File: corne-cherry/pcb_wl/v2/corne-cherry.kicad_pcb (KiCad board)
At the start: 2 copper layers, 152.8 x 91.4 mm, 72 parts, among them J1 MJ-4PP-9, J2 OLED, J3 Conn_01x02_Female, SW1 SW_PUSH, SW10 SW_PUSH, SW11 SW_PUSH, SW12 SW_PUSH, SW13 SW_PUSH, SW14 SW_PUSH, SW15 SW_PUSH, SW16 SW_PUSH, SW17 SW_PUSH, SW18 SW_PUSH, SW19 SW_PUSH, SW2 SW_PUSH, SW20 SW_PUSH, SW21 SW_PUSH, SW22 SW_PUSH, SW23 SW_SPDT, SW24 SW_SPDT, SW3 SW_PUSH, SW4 SW_PUSH, SW5 SW_PUSH, SW6 SW_PUSH, SW7 SW_PUSH, SW8 SW_PUSH, SW9 SW_PUSH, U1 ProMicro

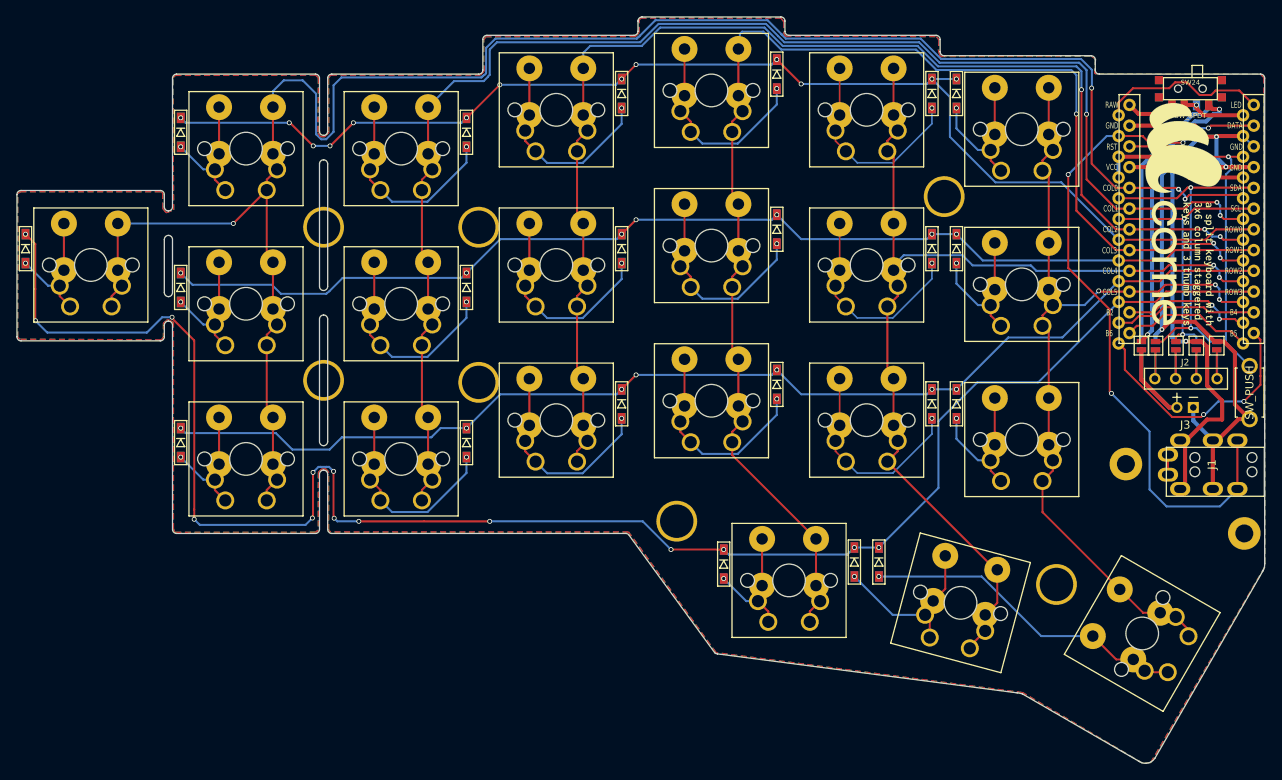
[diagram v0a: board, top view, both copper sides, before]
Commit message: Improver SI footprint, ground fills
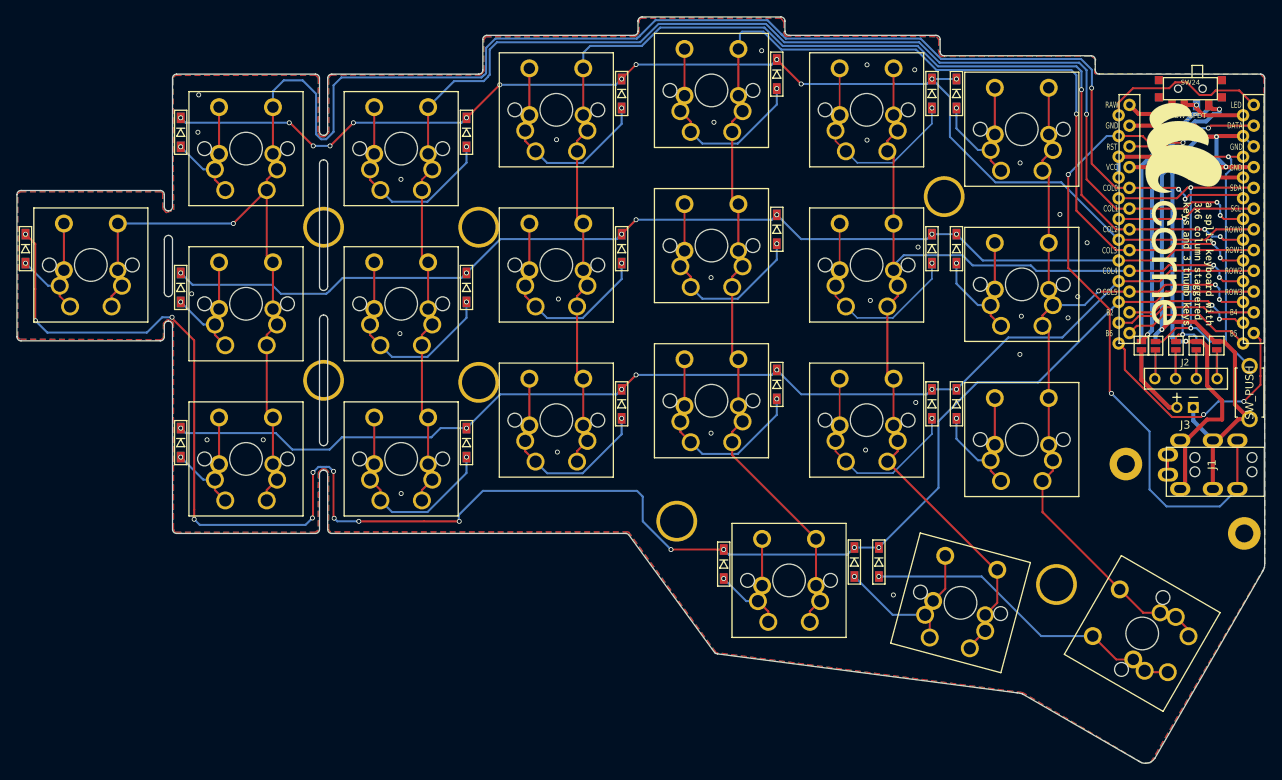
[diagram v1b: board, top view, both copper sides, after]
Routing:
- net row3: track 217.1 -> 222.5 mm
- net GND: vias 3 -> 33

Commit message: Added power switch stabilization vias
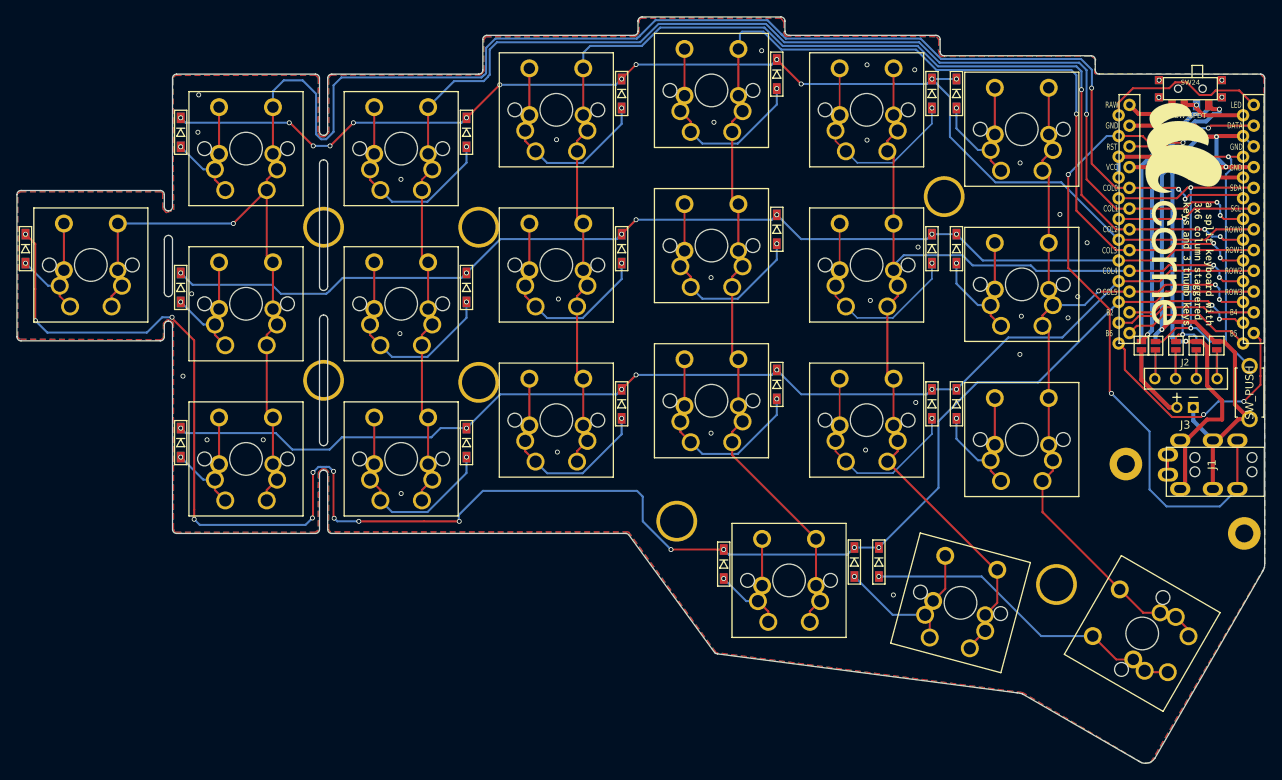
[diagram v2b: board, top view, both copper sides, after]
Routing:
- net GND: vias 33 -> 34
- net (no net): vias 0 -> 4
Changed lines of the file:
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@@
     (thickness 1.6)
     (drawings 110)
-    (tracks 989)
+    (tracks 994)
     (zones 0)
     (modules 72)
@@
   (gr_line (start 155 65.25) (end 155 63.75) (angle 90) (layer Edge.Cuts) (width 0.15))
   (gr_line (start 173.5 65.75) (end 155.5 65.75) (angle 90) (layer Edge.Cuts) (width 0.15))
+  (via (at 181.81308 68.74158) (size 0.6) (drill 0.4) (layers F.Cu B.Cu) (net 0))
+  (via (at 181.78768 70.84978) (size 0.6) (drill 0.4) (layers F.Cu B.Cu) (net 0))
+  (via (at 189.50928 70.82438) (size 0.6) (drill 0.4) (layers F.Cu B.Cu) (net 0))
+  (via (at 189.50928 68.74158) (size 0.6) (drill 0.4) (layers F.Cu B.Cu) (net 0))
   (segment (start 193.406 87.012) (end 193.4064 87.012) (width 0.25) (layer F.Cu) (net 1) (status 30))
   (segment (start 176.86 88.282) (end 187.518 88.282) (width 0.25) (layer F.Cu) (net 1) (status 10))
@@
   (via (at 172.99928 88.65518) (size 0.6) (drill 0.4) (layers F.Cu B.Cu) (net 26))
   (via (at 169.67188 85.17538) (size 0.6) (drill 0.4) (layers F.Cu B.Cu) (net 26))
+  (via (at 62.28068 104.98738) (size 0.6) (drill 0.4) (layers F.Cu B.Cu) (net 26))
   (segment (start 186.375 100.75) (end 187.05 100.75) (width 0.5) (layer F.Cu) (net 27) (status 10))
   (segment (start 187.05 100.75) (end 187.7 101.4) (width 0.5) (layer F.Cu) (net 27))

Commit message: flipped footprints
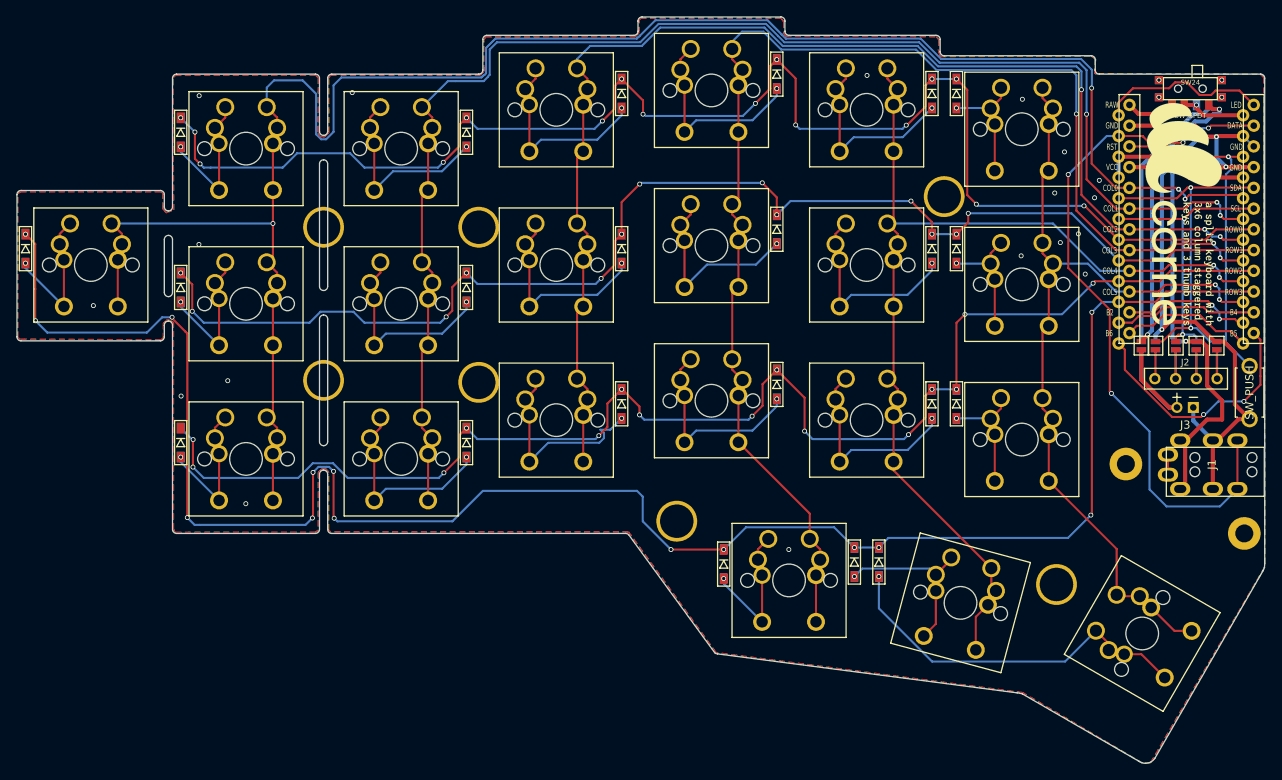
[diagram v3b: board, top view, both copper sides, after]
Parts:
- turned SW1 to 0 degrees
- turned SW10 to 0 degrees
- turned SW11 to 0 degrees
- turned SW12 to 0 degrees
- turned SW13 to 0 degrees
- turned SW14 to 0 degrees
- turned SW15 to 0 degrees
- turned SW16 to 0 degrees
- turned SW17 to 0 degrees
- turned SW18 to 0 degrees
- turned SW19 to 0 degrees
- turned SW2 to 0 degrees
- turned SW20 to 345 degrees
- turned SW21 to 60 degrees
- turned SW22 to 0 degrees
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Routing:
- net row2: track 144.0 -> 173.3 mm, vias 7 -> 15
- net row0: track 153.2 -> 180.5 mm, vias 13 -> 16
- net row1: track 139.8 -> 161.6 mm, vias 7 -> 13
- net row3: track 222.5 -> 233.6 mm
- net Net-(D21-Pad2): track 40.2 -> 46.0 mm
- net Net-(D12-Pad2): track 18.7 -> 15.1 mm
- net Net-(D6-Pad2): track 18.7 -> 15.1 mm
- net Net-(D18-Pad2): track 18.7 -> 15.1 mm
- net Net-(D19-Pad2): track 16.2 -> 18.1 mm
- net Net-(D22-Pad2): track 16.2 -> 18.1 mm
- net Net-(D7-Pad2): track 16.2 -> 18.1 mm
- net Net-(D13-Pad2): track 16.2 -> 18.1 mm
- net Net-(D1-Pad2): track 16.2 -> 18.1 mm
- net Net-(D2-Pad2): track 26.0 -> 24.4 mm
- net Net-(D10-Pad2): track 26.0 -> 24.4 mm
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
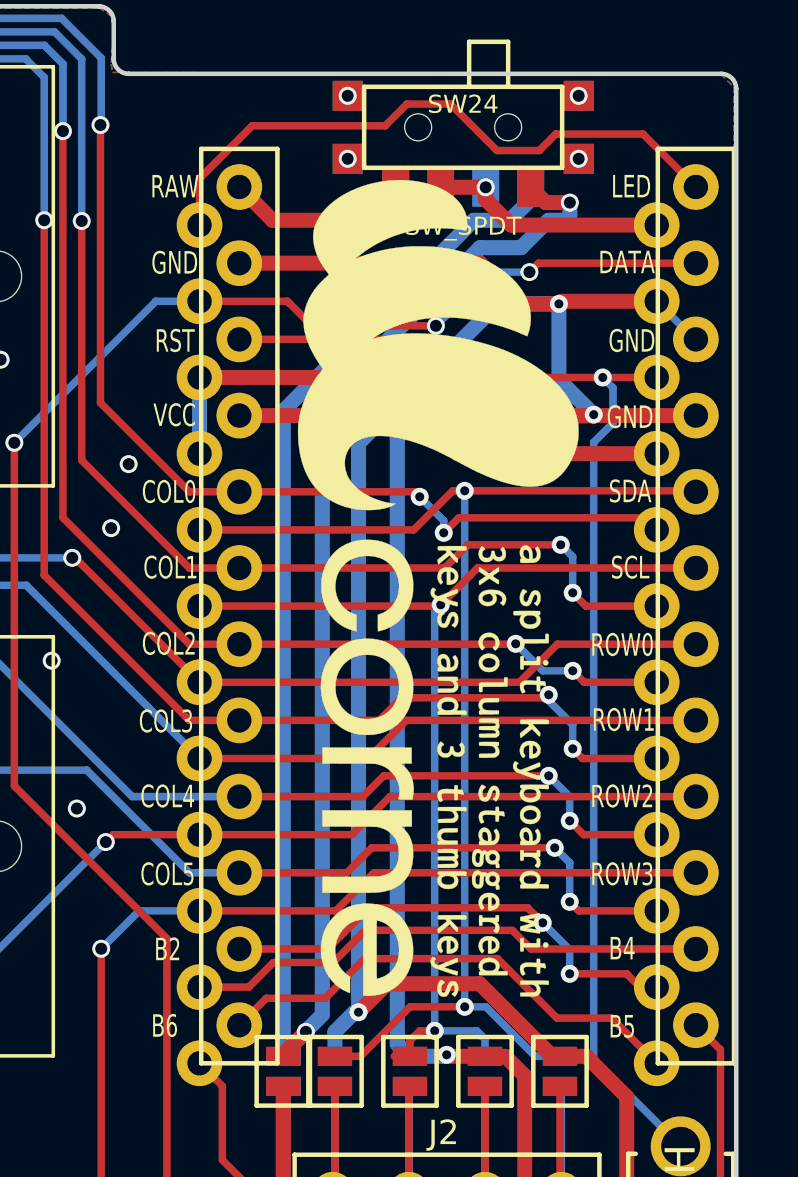
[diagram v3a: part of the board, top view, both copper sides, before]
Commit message: Added proper SPORNE logo
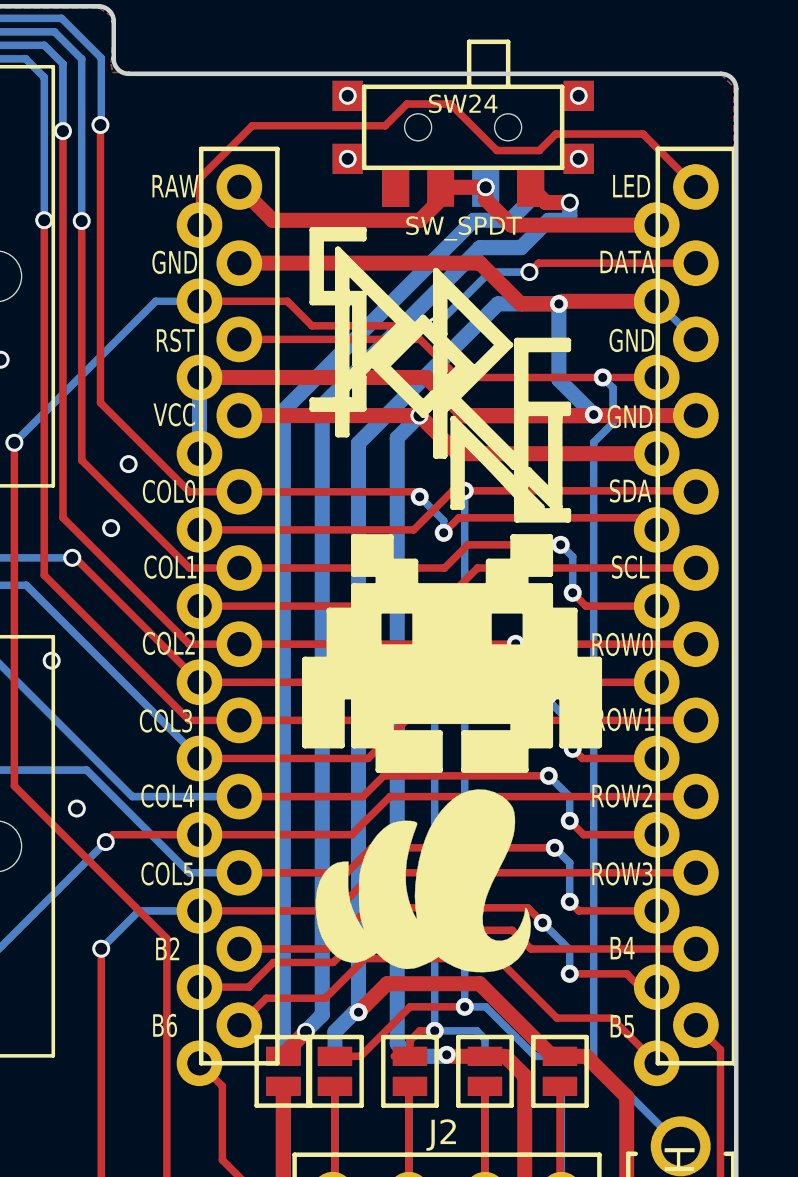
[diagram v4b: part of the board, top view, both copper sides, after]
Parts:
- added G***: LOGO, Silks:corne-logo, B.Cu at (183.9, 95.1)
- added G***: LOGO, Silks:corne-logo, F.Cu at (183.9, 95.1)
- added REF**: space-invader-logo, Silks:space-invader-logo, B.Cu at (185.1, 87.4)
- added REF**: space-invader-logo, Silks:space-invader-logo, F.Cu at (185.1, 87.4)
- G1, G2: footprint kbd:corne -> Silks:sporne-logo-small
- moved G1 6.69 mm to (185.1, 78.5), turned to 0 degrees
- moved G2 6.60 mm to (185.1, 78.5), turned to 180 degrees

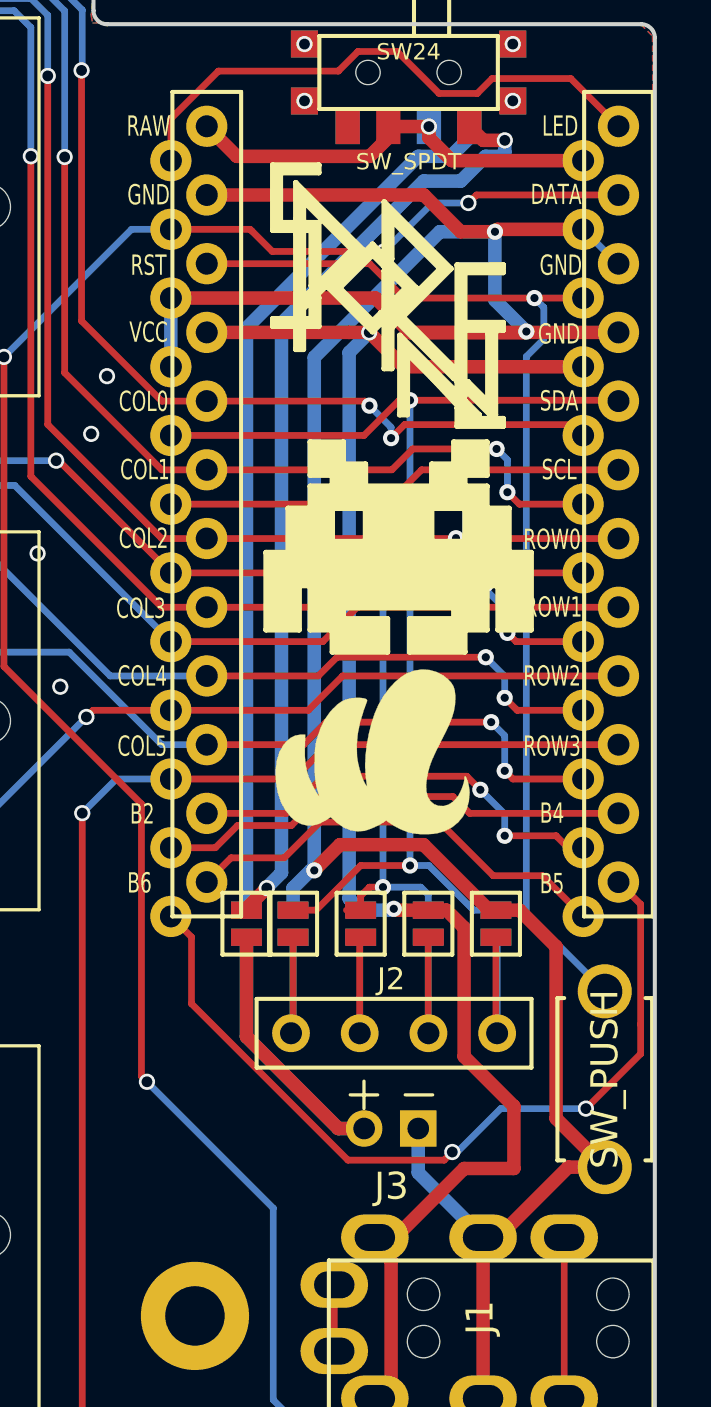
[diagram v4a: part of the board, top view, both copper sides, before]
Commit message: Logo fix
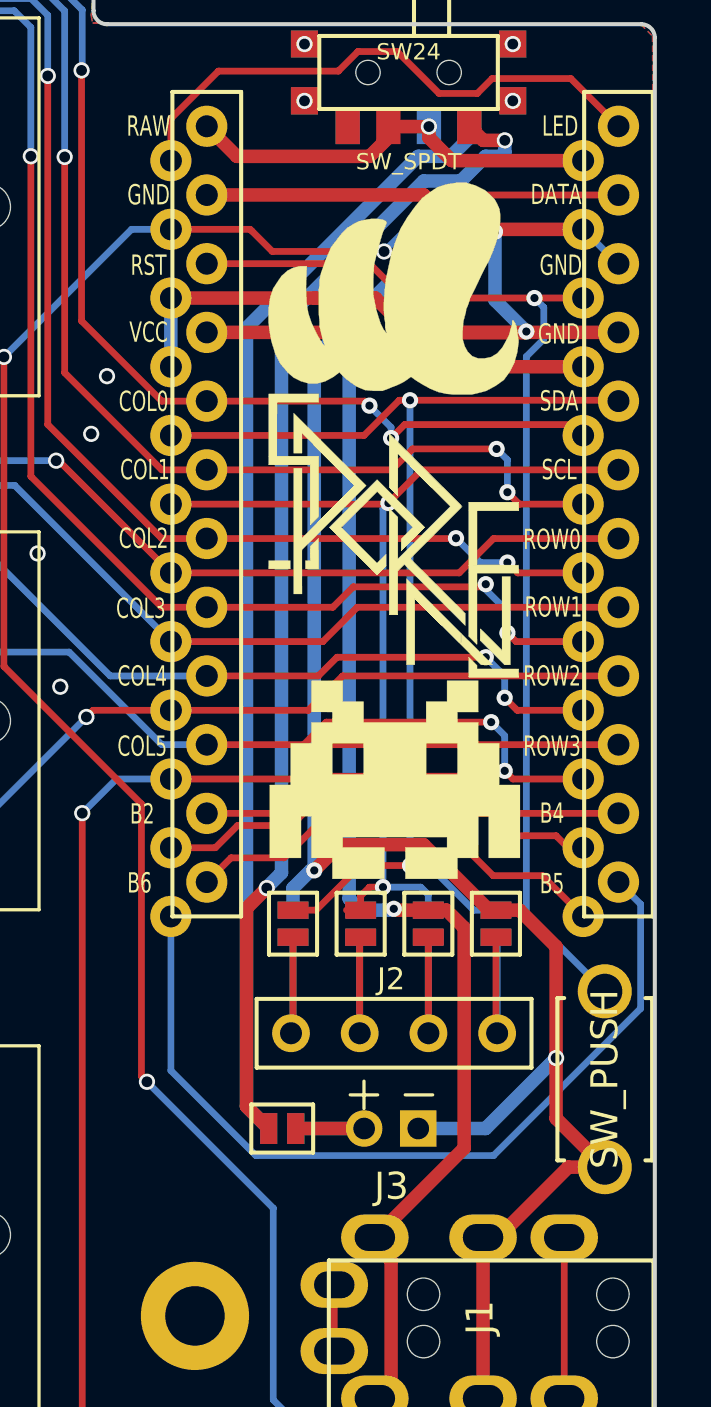
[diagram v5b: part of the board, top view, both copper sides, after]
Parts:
- removed the G*** at (183.9, 95.1) (x2)
- removed G1, G2: Logo_Open_Hardware_Small, Silks:sporne-logo-small
- removed REF** (x2): space-invader-logo, Silks:space-invader-logo
- added G***: LOGO, Silks:sporne-logo-small, B.Cu at (184.0, 86.8)
- added G***: LOGO, Silks:sporne-logo-small, F.Cu at (185.1, 86.7)
- moved JP1 7.69 mm to (181.0, 108.8), turned to 180 degrees
- moved JP10 7.69 mm to (181.0, 108.8), turned to 180 degrees
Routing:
- net Net-(J3-Pad2): track 18.9 -> 5.06 mm
- net Net-(JP10-Pad2): track 35.1 -> 43.5 mm
- net Net-(JP1-Pad2): track 33.1 -> 41.5 mm
- net VCC: track 62.7 -> 59.7 mm
- net GND: track 110.2 -> 111.4 mm, vias 21 -> 22
- net Net-(U1-Pad12): track 30.9 -> 31.6 mm, vias 2 -> 0

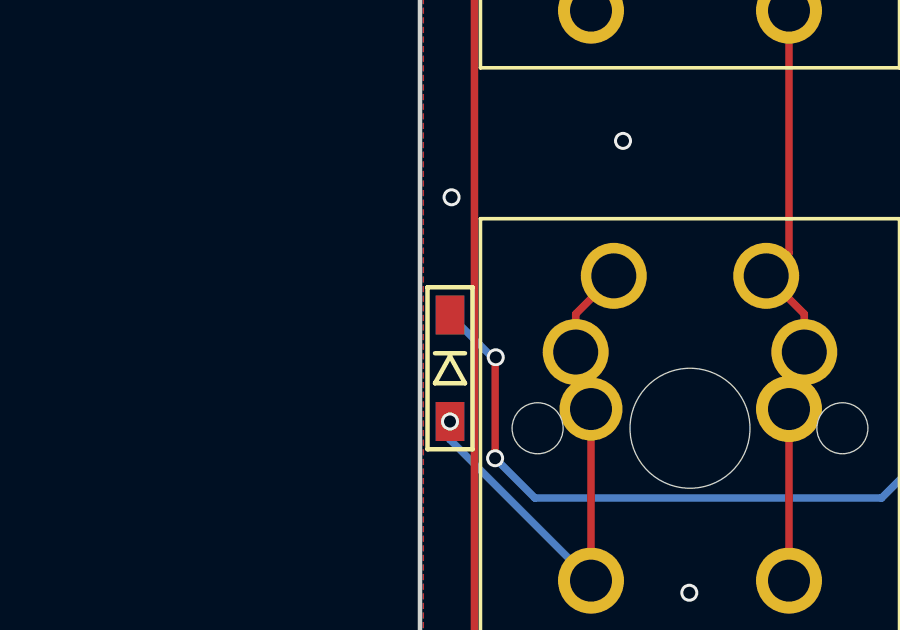
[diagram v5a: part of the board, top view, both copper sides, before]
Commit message: Diode via fix
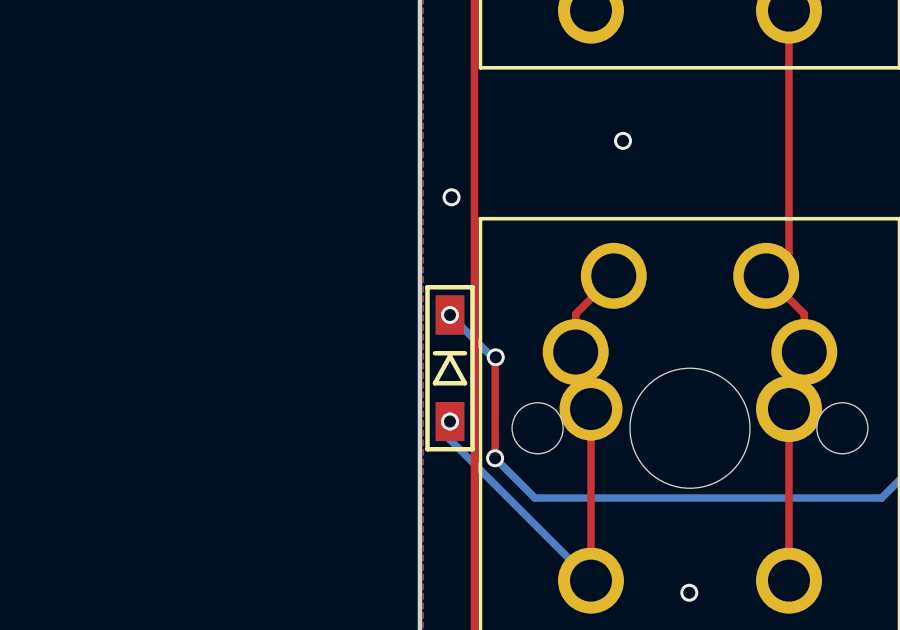
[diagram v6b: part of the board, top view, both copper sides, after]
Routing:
- net row2: vias 15 -> 16
